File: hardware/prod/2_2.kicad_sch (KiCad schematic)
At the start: 9 parts, among them U4 KH-TYPE-C-16P, U6 CH572D, X2 XTM20032000DT00351001

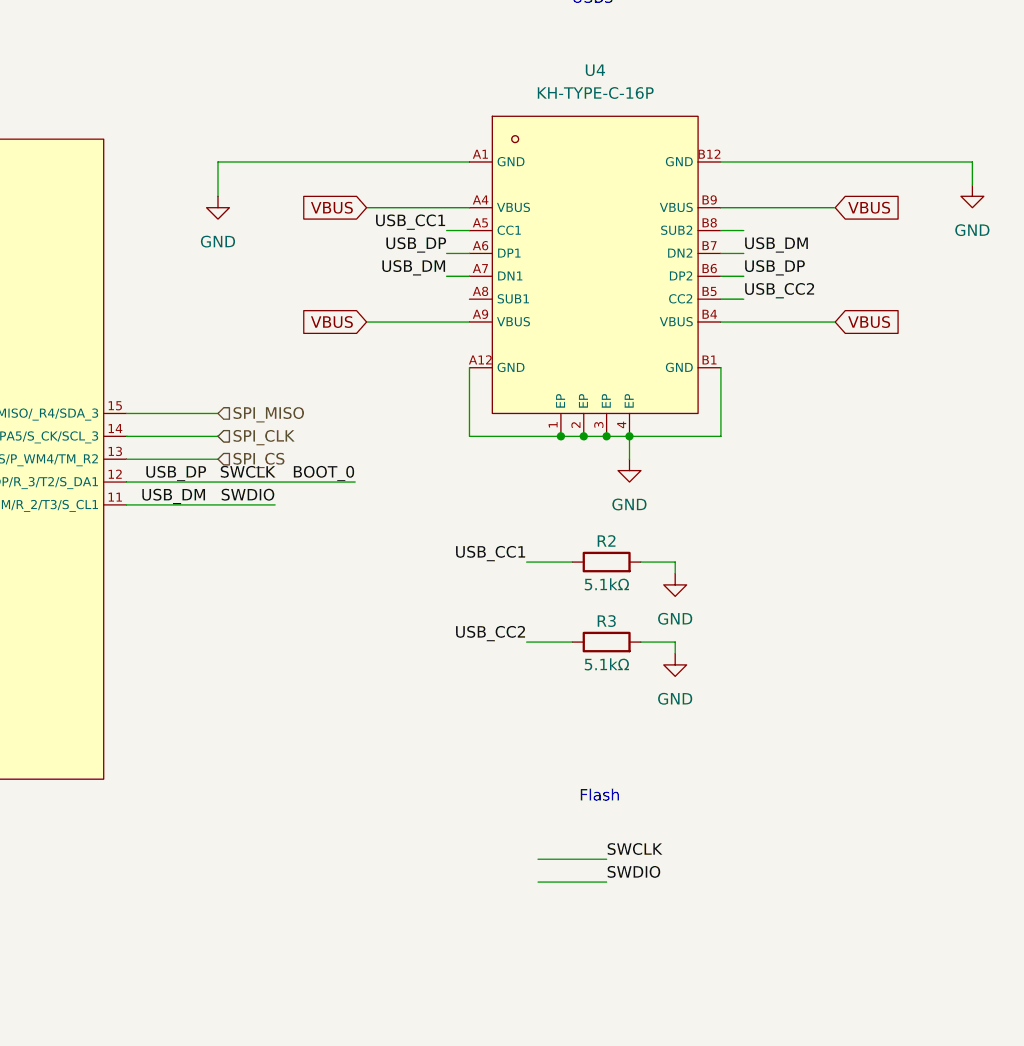
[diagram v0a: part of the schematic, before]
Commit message: feat(hardware-prod): replace mode transistors with TPS2121 power mux
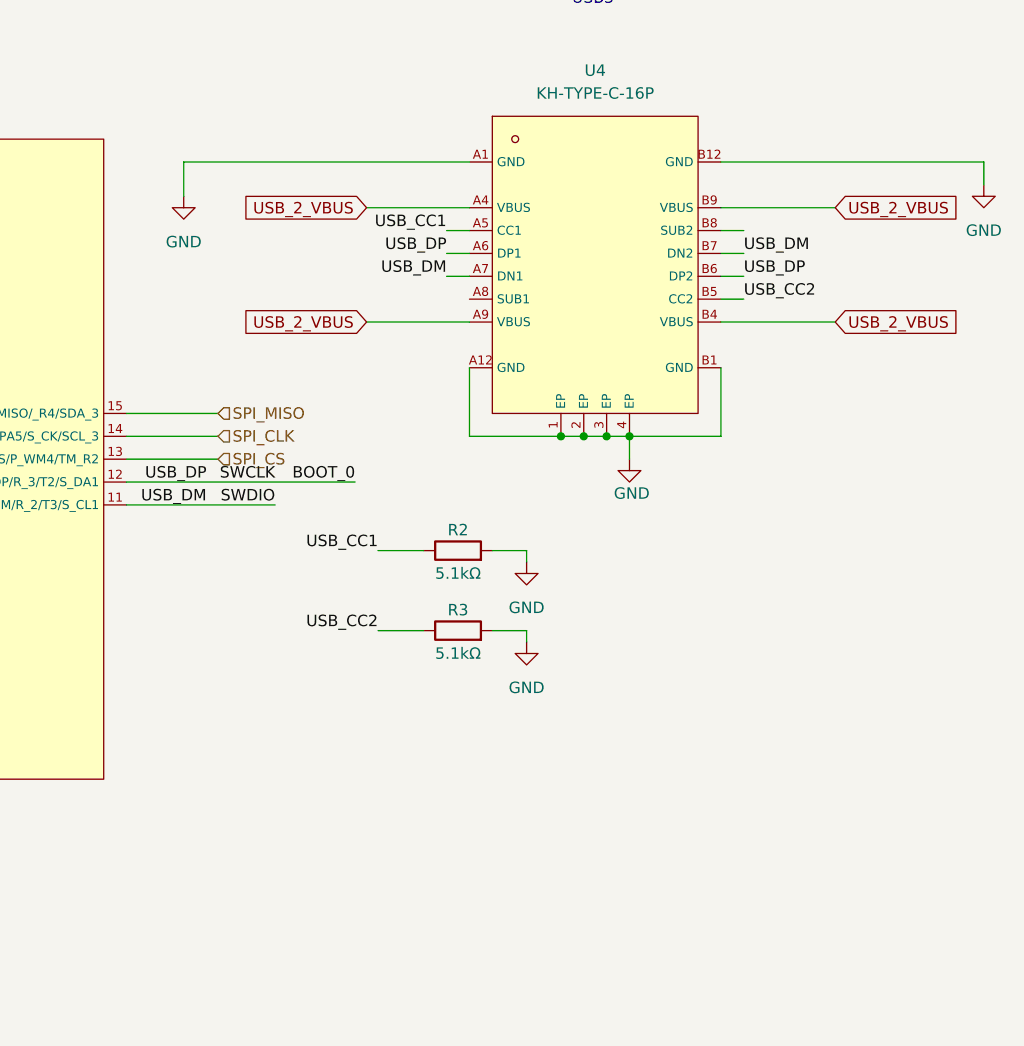
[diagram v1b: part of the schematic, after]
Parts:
- BOOT_1: value ~ -> (none)
- R1, R2, R3: footprint Resistor_SMD:R_0603_1608Metric -> Resistor_SMD:R_0402_1005Metric
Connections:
- net VBUS renamed USB_2_VBUS
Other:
- note removed: "Flash"
- moved on the sheet: R2, R3
